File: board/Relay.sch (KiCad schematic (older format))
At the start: 9 parts, among them K1 JS1-12V-F, K2 JS1-12V-F, K3 JS1-12V-F, K4 JS1-12V-F, U4 ULN2003A

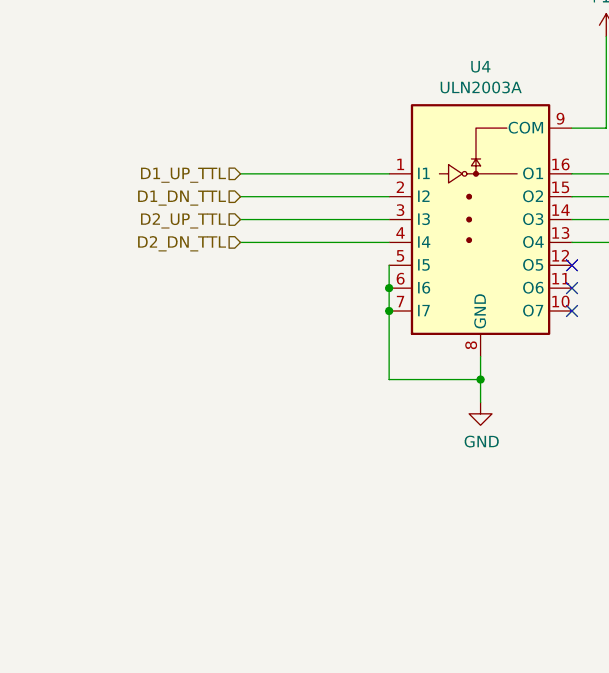
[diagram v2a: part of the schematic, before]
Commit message: Add relay status LEDs
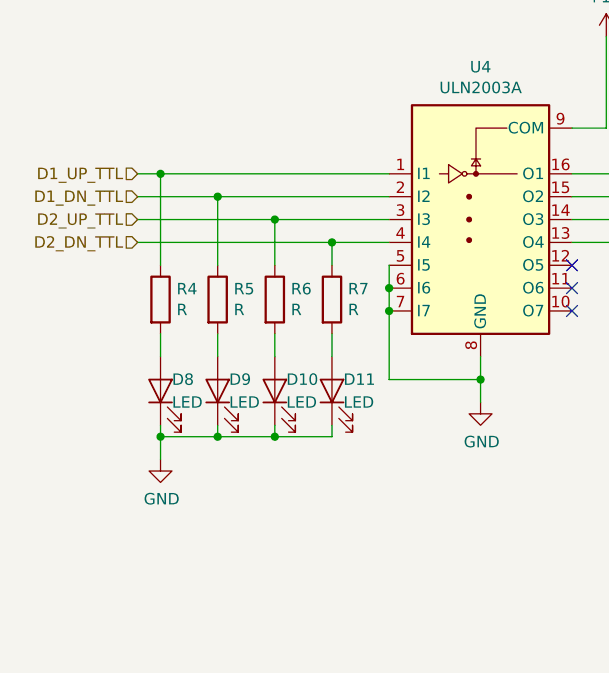
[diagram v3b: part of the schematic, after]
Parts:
- added D10, D11, D8, D9: LED, LEDs:LED_D3.0mm, symbol Device:LED
- added R4, R5, R6, R7: R, Resistors_THT:R_Axial_DIN0207_L6.3mm_D2.5mm_P10.16mm_Horizontal, symbol Device:R
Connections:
- net D1_DN_TTL: now also R5.1
- net D1_UP_TTL: now also R4.1
- net D2_DN_TTL: now also R7.1
- net D2_UP_TTL: now also R6.1
- net GND: now also D10.1 (K), D11.1 (K), D8.1 (K), D9.1 (K)
- new net: D11.2 (A), R7.2
- new net: D10.2 (A), R6.2
- new net: D9.2 (A), R5.2
- new net: D8.2 (A), R4.2
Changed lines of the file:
@@
 	1    0    0    -1
 $EndComp
-Text HLabel 1500 2500 0    50   Input ~ 0
+Text HLabel 1050 2500 0    50   Input ~ 0
 D1_UP_TTL
-Text HLabel 1500 2600 0    50   Input ~ 0
+Text HLabel 1050 2600 0    50   Input ~ 0
 D1_DN_TTL
-Text HLabel 1500 2700 0    50   Input ~ 0
+Text HLabel 1050 2700 0    50   Input ~ 0
 D2_UP_TTL
-Text HLabel 1500 2800 0    50   Input ~ 0
+Text HLabel 1050 2800 0    50   Input ~ 0
 D2_DN_TTL
-Wire Wire Line
-	1500 2500 2150 2500
-Wire Wire Line
-	1500 2600 2150 2600
-Wire Wire Line
-	1500 2700 2150 2700
-Wire Wire Line
-	1500 2800 2150 2800
 $Comp
 L power:GND #PWR0106
@@
 Wire Wire Line
 	7850 3300 7850 4300
+Wire Wire Line
+	1050 2500 1150 2500
+Wire Wire Line
+	1050 2600 1400 2600
+Wire Wire Line
+	1050 2700 1650 2700
+Wire Wire Line
+	1050 2800 1900 2800
+$Comp
+L Device:R R7
+U 1 1 5D6E4821
+P 1900 3050
+F 0 "R7" H 1970 3096 50  0000 L CNN
+F 1 "R" H 1970 3005 50  0000 L CNN
+F 2 "Resistors_THT:R_Axial_DIN0207_L6.3mm_D2.5mm_P10.16mm_Horizontal" V 1830 3050 50  0001 C CNN
+F 3 "~" H 1900 3050 50  0001 C CNN
+	1    1900 3050
+	1    0    0    -1
+$EndComp
+$Comp
+L Device:R R6
+U 1 1 5D6E54AB
+P 1650 3050
+F 0 "R6" H 1720 3096 50  0000 L CNN
+F 1 "R" H 1720 3005 50  0000 L CNN
+F 2 "Resistors_THT:R_Axial_DIN0207_L6.3mm_D2.5mm_P10.16mm_Horizontal" V 1580 3050 50  0001 C CNN
+F 3 "~" H 1650 3050 50  0001 C CNN
+	1    1650 3050
+	1    0    0    -1
+$EndComp
+$Comp
+L Device:R R5
+U 1 1 5D6E6CF6
+P 1400 3050
+F 0 "R5" H 1470 3096 50  0000 L CNN
+F 1 "R" H 1470 3005 50  0000 L CNN
+F 2 "Resistors_THT:R_Axial_DIN0207_L6.3mm_D2.5mm_P10.16mm_Horizontal" V 1330 3050 50  0001 C CNN
+F 3 "~" H 1400 3050 50  0001 C CNN
+	1    1400 3050
+	1    0    0    -1
+$EndComp
+$Comp
+L Device:R R4
+U 1 1 5D6E8437
+P 1150 3050
+F 0 "R4" H 1220 3096 50  0000 L CNN
+F 1 "R" H 1220 3005 50  0000 L CNN
+F 2 "Resistors_THT:R_Axial_DIN0207_L6.3mm_D2.5mm_P10.16mm_Horizontal" V 1080 3050 50  0001 C CNN
+F 3 "~" H 1150 3050 50  0001 C CNN
+	1    1150 3050
+	1    0    0    -1
+$EndComp
+$Comp
+L Device:LED D8
+U 1 1 5D6E9A8E
+P 1150 3450
+F 0 "D8" V 1200 3400 50  0000 R CNN
+F 1 "LED" V 1100 3400 50  0000 R CNN
+F 2 "LEDs:LED_D3.0mm" H 1150 3450 50  0001 C CNN
+F 3 "~" H 1150 3450 50  0001 C CNN
+	1    1150 3450
+	0    -1   -1   0
+$EndComp
+$Comp
+L Device:LED D9
+U 1 1 5D6EA810
+P 1400 3450
+F 0 "D9" V 1450 3400 50  0000 R CNN
+F 1 "LED" V 1350 3400 50  0000 R CNN
+F 2 "LEDs:LED_D3.0mm" H 1400 3450 50  0001 C CNN
+F 3 "~" H 1400 3450 50  0001 C CNN
+	1    1400 3450
+	0    -1   -1   0
+$EndComp
+$Comp
+L Device:LED D10
+U 1 1 5D6EC3F0
+P 1650 3450
+F 0 "D10" V 1700 3400 50  0000 R CNN
+F 1 "LED" V 1600 3400 50  0000 R CNN
+F 2 "LEDs:LED_D3.0mm" H 1650 3450 50  0001 C CNN
+F 3 "~" H 1650 3450 50  0001 C CNN
+	1    1650 3450
+	0    -1   -1   0
+$EndComp
+$Comp
+L Device:LED D11
+U 1 1 5D6EE0A2
+P 1900 3450
+F 0 "D11" V 1950 3400 50  0000 R CNN
+F 1 "LED" V 1850 3400 50  0000 R CNN
+F 2 "LEDs:LED_D3.0mm" H 1900 3450 50  0001 C CNN
+F 3 "~" H 1900 3450 50  0001 C CNN
+	1    1900 3450
+	0    -1   -1   0
+$EndComp
+Wire Wire Line
+	1150 2500 1150 2900
+Connection ~ 1150 2500
+Wire Wire Line
+	1150 2500 2150 2500
+Wire Wire Line
+	1400 2600 1400 2900
+Connection ~ 1400 2600
+Wire Wire Line
+	1400 2600 2150 2600
+Wire Wire Line
+	1650 2700 1650 2900
+Connection ~ 1650 2700
+Wire Wire Line
+	1650 2700 2150 2700
+Wire Wire Line
+	1900 2800 1900 2900
+Connection ~ 1900 2800
+Wire Wire Line
+	1900 2800 2150 2800
+Wire Wire Line
+	1150 3200 1150 3300
+Wire Wire Line
+	1400 3200 1400 3300
+Wire Wire Line
+	1650 3200 1650 3300
+Wire Wire Line
+	1900 3200 1900 3300
+$Comp
+L power:GND #PWR0110
+U 1 1 5D700BE5
+P 1150 3750
+F 0 "#PWR0110" H 1150 3500 50  0001 C CNN
+F 1 "GND" H 1155 3577 50  0000 C CNN
+F 2 "" H 1150 3750 50  0001 C CNN
+F 3 "" H 1150 3750 50  0001 C CNN
+	1    1150 3750
+	1    0    0    -1
+$EndComp
+Wire Wire Line
+	1150 3600 1150 3650
+Wire Wire Line
+	1400 3600 1400 3650
+Wire Wire Line
+	1400 3650 1150 3650
+Connection ~ 1150 3650
+Wire Wire Line
+	1150 3650 1150 3750
+Wire Wire Line
+	1650 3600 1650 3650
+Wire Wire Line
+	1650 3650 1400 3650
+Connection ~ 1400 3650
+Wire Wire Line
+	1900 3600 1900 3650
+Wire Wire Line
+	1900 3650 1650 3650
+Connection ~ 1650 3650
 $EndSCHEMATC

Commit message: Add nominal LED R values; ground plane tweaks; first board spin
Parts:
- R4, R5, R6, R7: value R -> 150R
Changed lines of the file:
@@
 P 1900 3050
 F 0 "R7" H 1970 3096 50  0000 L CNN
-F 1 "R" H 1970 3005 50  0000 L CNN
+F 1 "150R" V 1900 2950 50  0000 L CNN
 F 2 "Resistors_THT:R_Axial_DIN0207_L6.3mm_D2.5mm_P10.16mm_Horizontal" V 1830 3050 50  0001 C CNN
 F 3 "~" H 1900 3050 50  0001 C CNN
@@
 P 1650 3050
 F 0 "R6" H 1720 3096 50  0000 L CNN
-F 1 "R" H 1720 3005 50  0000 L CNN
+F 1 "150R" V 1650 2950 50  0000 L CNN
 F 2 "Resistors_THT:R_Axial_DIN0207_L6.3mm_D2.5mm_P10.16mm_Horizontal" V 1580 3050 50  0001 C CNN
 F 3 "~" H 1650 3050 50  0001 C CNN
@@
 P 1400 3050
 F 0 "R5" H 1470 3096 50  0000 L CNN
-F 1 "R" H 1470 3005 50  0000 L CNN
+F 1 "150R" V 1400 2950 50  0000 L CNN
 F 2 "Resistors_THT:R_Axial_DIN0207_L6.3mm_D2.5mm_P10.16mm_Horizontal" V 1330 3050 50  0001 C CNN
 F 3 "~" H 1400 3050 50  0001 C CNN
@@
 P 1150 3050
 F 0 "R4" H 1220 3096 50  0000 L CNN
-F 1 "R" H 1220 3005 50  0000 L CNN
+F 1 "150R" V 1150 2950 50  0000 L CNN
 F 2 "Resistors_THT:R_Axial_DIN0207_L6.3mm_D2.5mm_P10.16mm_Horizontal" V 1080 3050 50  0001 C CNN
 F 3 "~" H 1150 3050 50  0001 C CNN

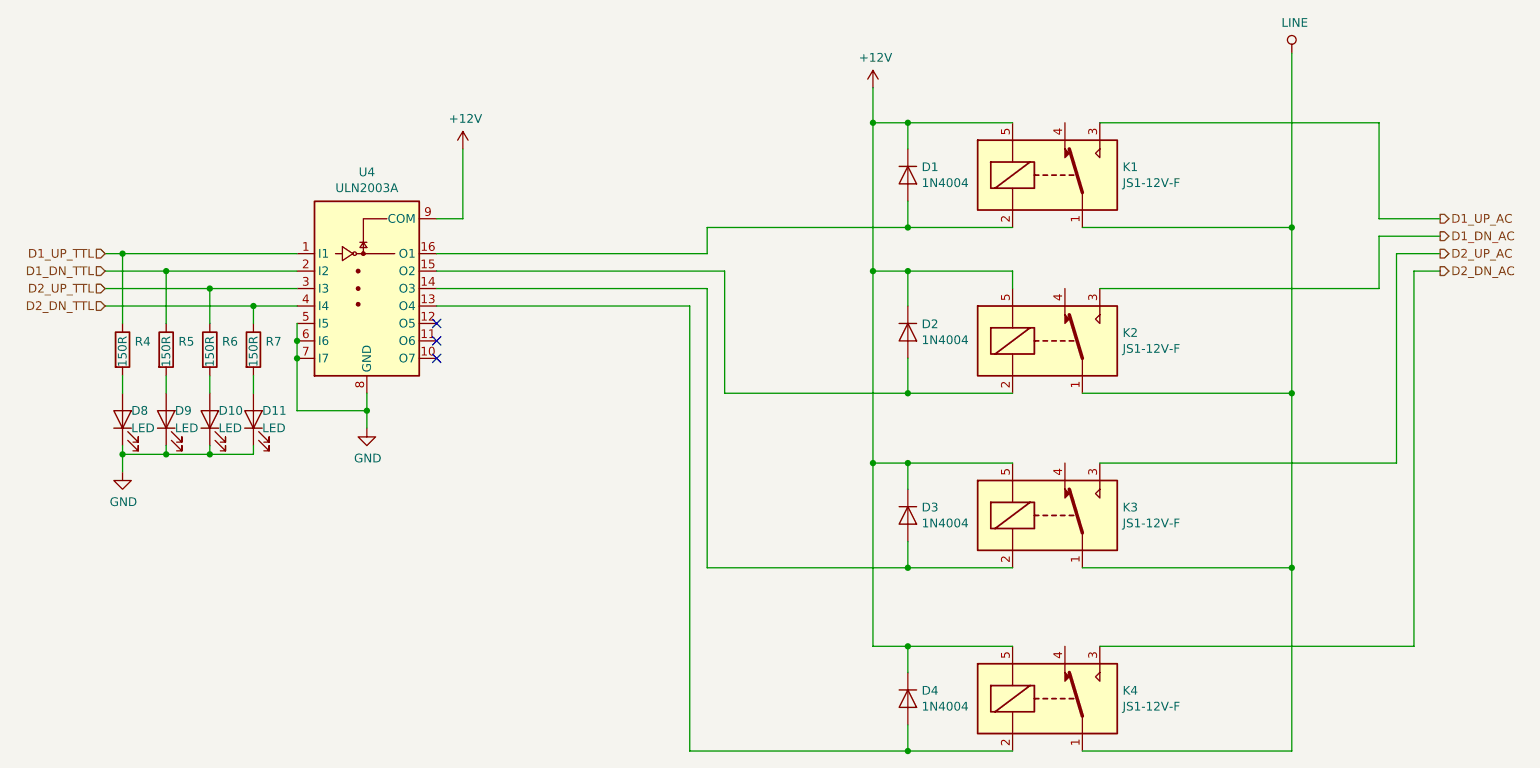
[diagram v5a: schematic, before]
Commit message: Minor layout tweaks, component updates
* Add an MCU driven status LED
* Update LED current limit resistor values
* Minor trace tweaks for clearance
* Based on empirical measurements of rev 0.1 board, adjust the location of the
  board mounting holes.
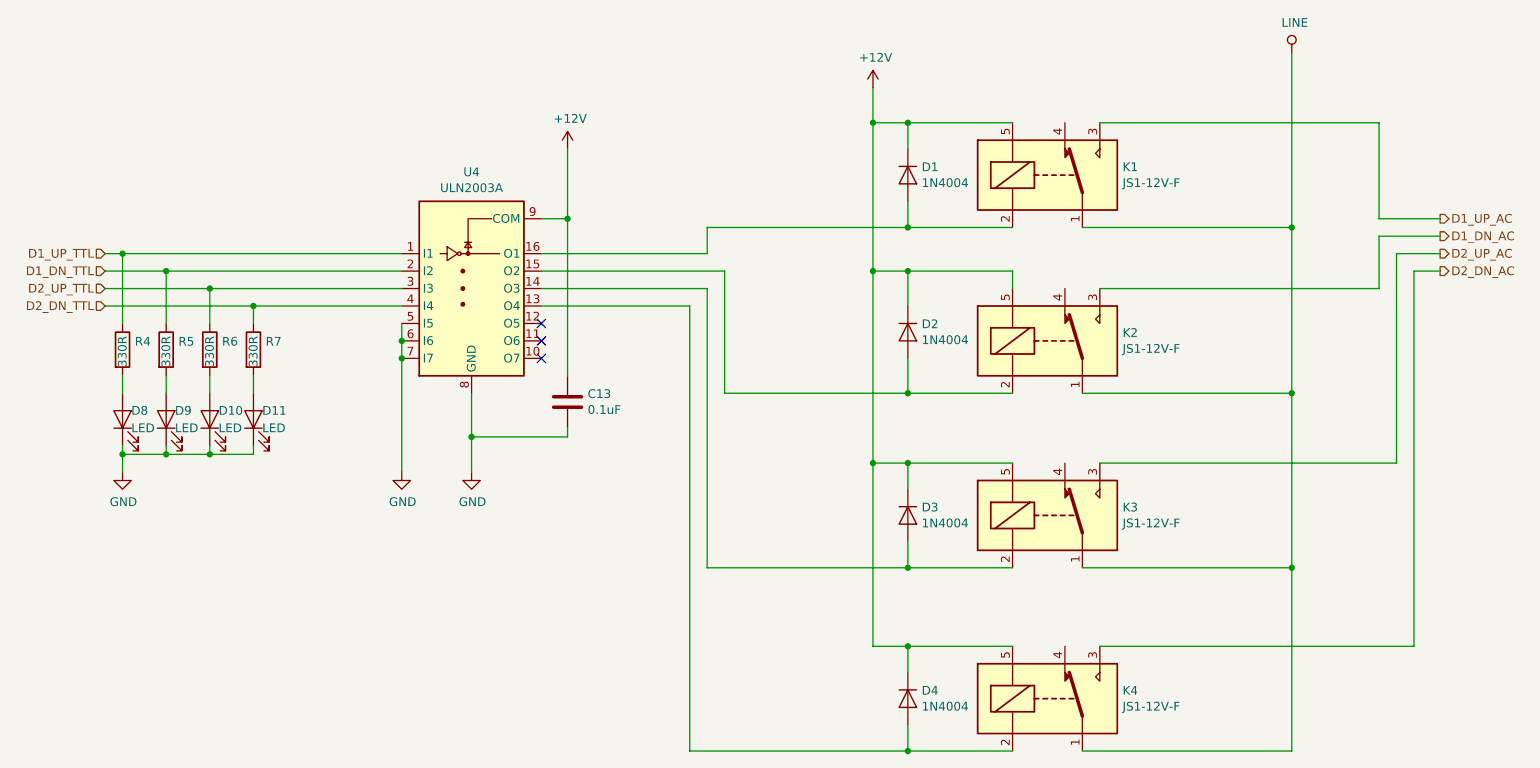
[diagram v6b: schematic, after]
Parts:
- added C13: 0.1uF, Capacitors_THT:C_Disc_D5.0mm_W2.5mm_P2.50mm, symbol Device:C
- R4, R5, R6, R7: value 150R -> 330R
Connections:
- net +12V: now also C13.1
- net GND: now also C13.2
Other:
- moved on the sheet: U4
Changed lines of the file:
@@
 L Transistor_Array:ULN2003A U4
 U 1 1 5D6FD156
-P 2550 2700
-F 0 "U4" H 2550 3367 50  0000 C CNN
-F 1 "ULN2003A" H 2550 3276 50  0000 C CNN
-F 2 "Housings_DIP:DIP-16_W7.62mm_LongPads" H 2600 2150 50  0001 L CNN
-F 3 "http://www.ti.com/lit/ds/symlink/uln2003a.pdf" H 2650 2500 50  0001 C CNN
-	1    2550 2700
+P 3150 2700
+F 0 "U4" H 3150 3367 50  0000 C CNN
+F 1 "ULN2003A" H 3150 3276 50  0000 C CNN
+F 2 "Housings_DIP:DIP-16_W7.62mm_LongPads" H 3200 2150 50  0001 L CNN
+F 3 "http://www.ti.com/lit/ds/symlink/uln2003a.pdf" H 3250 2500 50  0001 C CNN
+	1    3150 2700
 	1    0    0    -1
 $EndComp
@@
 L power:GND #PWR0106
 U 1 1 5D7017FB
-P 2550 3500
-F 0 "#PWR0106" H 2550 3250 50  0001 C CNN
-F 1 "GND" H 2555 3327 50  0000 C CNN
-F 2 "" H 2550 3500 50  0001 C CNN
-F 3 "" H 2550 3500 50  0001 C CNN
-	1    2550 3500
-	1    0    0    -1
-$EndComp
-Wire Wire Line
-	2550 3300 2550 3400
+P 3150 3750
+F 0 "#PWR0106" H 3150 3500 50  0001 C CNN
+F 1 "GND" H 3155 3577 50  0000 C CNN
+F 2 "" H 3150 3750 50  0001 C CNN
+F 3 "" H 3150 3750 50  0001 C CNN
+	1    3150 3750
+	1    0    0    -1
+$EndComp
 $Comp
 L power:+12V #PWR0107
 U 1 1 5D701C71
-P 3100 1900
-F 0 "#PWR0107" H 3100 1750 50  0001 C CNN
-F 1 "+12V" H 3115 2073 50  0000 C CNN
-F 2 "" H 3100 1900 50  0001 C CNN
-F 3 "" H 3100 1900 50  0001 C CNN
-	1    3100 1900
-	1    0    0    -1
-$EndComp
-Wire Wire Line
-	2950 2300 3100 2300
-Wire Wire Line
-	3100 2300 3100 1900
-Wire Wire Line
-	2150 2900 2150 3000
-Wire Wire Line
-	2150 3000 2150 3100
-Connection ~ 2150 3000
-Wire Wire Line
-	2150 3100 2150 3400
-Wire Wire Line
-	2150 3400 2550 3400
-Connection ~ 2150 3100
-Connection ~ 2550 3400
-Wire Wire Line
-	2550 3400 2550 3500
-NoConn ~ 2950 2900
-NoConn ~ 2950 3000
-NoConn ~ 2950 3100
+P 3700 1900
+F 0 "#PWR0107" H 3700 1750 50  0001 C CNN
+F 1 "+12V" H 3715 2073 50  0000 C CNN
+F 2 "" H 3700 1900 50  0001 C CNN
+F 3 "" H 3700 1900 50  0001 C CNN
+	1    3700 1900
+	1    0    0    -1
+$EndComp
+Wire Wire Line
+	3550 2300 3700 2300
+Wire Wire Line
+	3700 2300 3700 1900
+Wire Wire Line
+	2750 2900 2750 3000
+Wire Wire Line
+	2750 3000 2750 3100
+Connection ~ 2750 3000
+NoConn ~ 3550 2900
+NoConn ~ 3550 3000
+NoConn ~ 3550 3100
 Text HLabel 8700 2300 2    50   Output ~ 0
 D1_UP_AC
@@
 	6250 2350 5650 2350
 Wire Wire Line
-	2950 2500 4500 2500
-Wire Wire Line
 	6250 2600 6250 2700
-Wire Wire Line
-	2950 2700 4500 2700
-Wire Wire Line
-	2950 2800 4400 2800
 $Comp
 L Diode:1N4004 D1
@@
 Wire Wire Line
 	4600 3300 4600 2600
-Wire Wire Line
-	4600 2600 2950 2600
 Connection ~ 5650 3300
 $Comp
@@
 P 1900 3050
 F 0 "R7" H 1970 3096 50  0000 L CNN
-F 1 "150R" V 1900 2950 50  0000 L CNN
+F 1 "330R" V 1900 2950 50  0000 L CNN
 F 2 "Resistors_THT:R_Axial_DIN0207_L6.3mm_D2.5mm_P10.16mm_Horizontal" V 1830 3050 50  0001 C CNN
 F 3 "~" H 1900 3050 50  0001 C CNN
@@
 P 1650 3050
 F 0 "R6" H 1720 3096 50  0000 L CNN
-F 1 "150R" V 1650 2950 50  0000 L CNN
+F 1 "330R" V 1650 2950 50  0000 L CNN
 F 2 "Resistors_THT:R_Axial_DIN0207_L6.3mm_D2.5mm_P10.16mm_Horizontal" V 1580 3050 50  0001 C CNN
 F 3 "~" H 1650 3050 50  0001 C CNN
@@
 P 1400 3050
 F 0 "R5" H 1470 3096 50  0000 L CNN
-F 1 "150R" V 1400 2950 50  0000 L CNN
+F 1 "330R" V 1400 2950 50  0000 L CNN
 F 2 "Resistors_THT:R_Axial_DIN0207_L6.3mm_D2.5mm_P10.16mm_Horizontal" V 1330 3050 50  0001 C CNN
 F 3 "~" H 1400 3050 50  0001 C CNN
 	1    1400 3050
-	1    0    0    -1
-$EndComp
-$Comp
-L Device:R R4
-U 1 1 5D6E8437
-P 1150 3050
-F 0 "R4" H 1220 3096 50  0000 L CNN
-F 1 "150R" V 1150 2950 50  0000 L CNN
-F 2 "Resistors_THT:R_Axial_DIN0207_L6.3mm_D2.5mm_P10.16mm_Horizontal" V 1080 3050 50  0001 C CNN
-F 3 "~" H 1150 3050 50  0001 C CNN
-	1    1150 3050
 	1    0    0    -1
 $EndComp
@@
 Wire Wire Line
 	1150 2500 1150 2900
-Connection ~ 1150 2500
-Wire Wire Line
-	1150 2500 2150 2500
 Wire Wire Line
 	1400 2600 1400 2900
-Connection ~ 1400 2600
-Wire Wire Line
-	1400 2600 2150 2600
 Wire Wire Line
 	1650 2700 1650 2900
-Connection ~ 1650 2700
-Wire Wire Line
-	1650 2700 2150 2700
 Wire Wire Line
 	1900 2800 1900 2900
-Connection ~ 1900 2800
-Wire Wire Line
-	1900 2800 2150 2800
 Wire Wire Line
 	1150 3200 1150 3300
@@
 	1900 3650 1650 3650
 Connection ~ 1650 3650
+$Comp
+L Device:R R4
+U 1 1 5D6E8437
+P 1150 3050
+F 0 "R4" H 1220 3096 50  0000 L CNN
+F 1 "330R" V 1150 2950 50  0000 L CNN
+F 2 "Resistors_THT:R_Axial_DIN0207_L6.3mm_D2.5mm_P10.16mm_Horizontal" V 1080 3050 50  0001 C CNN
+F 3 "~" H 1150 3050 50  0001 C CNN
+	1    1150 3050
+	1    0    0    -1
+$EndComp
+$Comp
+L power:GND #PWR0112
+U 1 1 5D758D65
+P 2750 3750
+F 0 "#PWR0112" H 2750 3500 50  0001 C CNN
+F 1 "GND" H 2755 3577 50  0000 C CNN
+F 2 "" H 2750 3750 50  0001 C CNN
+F 3 "" H 2750 3750 50  0001 C CNN
+	1    2750 3750
+	1    0    0    -1
+$EndComp
+Wire Wire Line
+	3150 3300 3150 3550
+Wire Wire Line
+	2750 3100 2750 3750
+Connection ~ 2750 3100
+Wire Wire Line
+	3550 2500 4500 2500
+Wire Wire Line
+	3550 2600 4600 2600
+Wire Wire Line
+	3550 2700 4500 2700
+Wire Wire Line
+	3550 2800 4400 2800
+Wire Wire Line
+	2750 2500 1150 2500
+Connection ~ 1150 2500
+Wire Wire Line
+	2750 2600 1400 2600
+Connection ~ 1400 2600
+Wire Wire Line
+	2750 2700 1650 2700
+Connection ~ 1650 2700
+Wire Wire Line
+	2750 2800 1900 2800
+Connection ~ 1900 2800
+$Comp
+L Device:C C13
+U 1 1 5D7871B3
+P 3700 3350
+F 0 "C13" H 3815 3396 50  0000 L CNN
+F 1 "0.1uF" H 3815 3305 50  0000 L CNN
+F 2 "Capacitors_THT:C_Disc_D5.0mm_W2.5mm_P2.50mm" H 3738 3200 50  0001 C CNN
+F 3 "~" H 3700 3350 50  0001 C CNN
+	1    3700 3350
+	1    0    0    -1
+$EndComp
+Wire Wire Line
+	3700 2300 3700 3200
+Connection ~ 3700 2300
+Wire Wire Line
+	3700 3500 3700 3550
+Wire Wire Line
+	3700 3550 3150 3550
+Connection ~ 3150 3550
+Wire Wire Line
+	3150 3550 3150 3750
 $EndSCHEMATC

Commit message: Split the 5v and 12v ground paths
* To control the return path for (noisy) relay current, split the grounds for
  the 12v and 5v sections.
* The grounds are joined by bridges (solder pads) placed adjacent to the 5v
  regulator, on both layers.
* The gound plane is split in two; conveniently the 12v vs 5v components were
  already well placed to make this straightforward.
* 12v power LED uses the 5v ground to simplify routing.
* Add dummy power flags for ERC
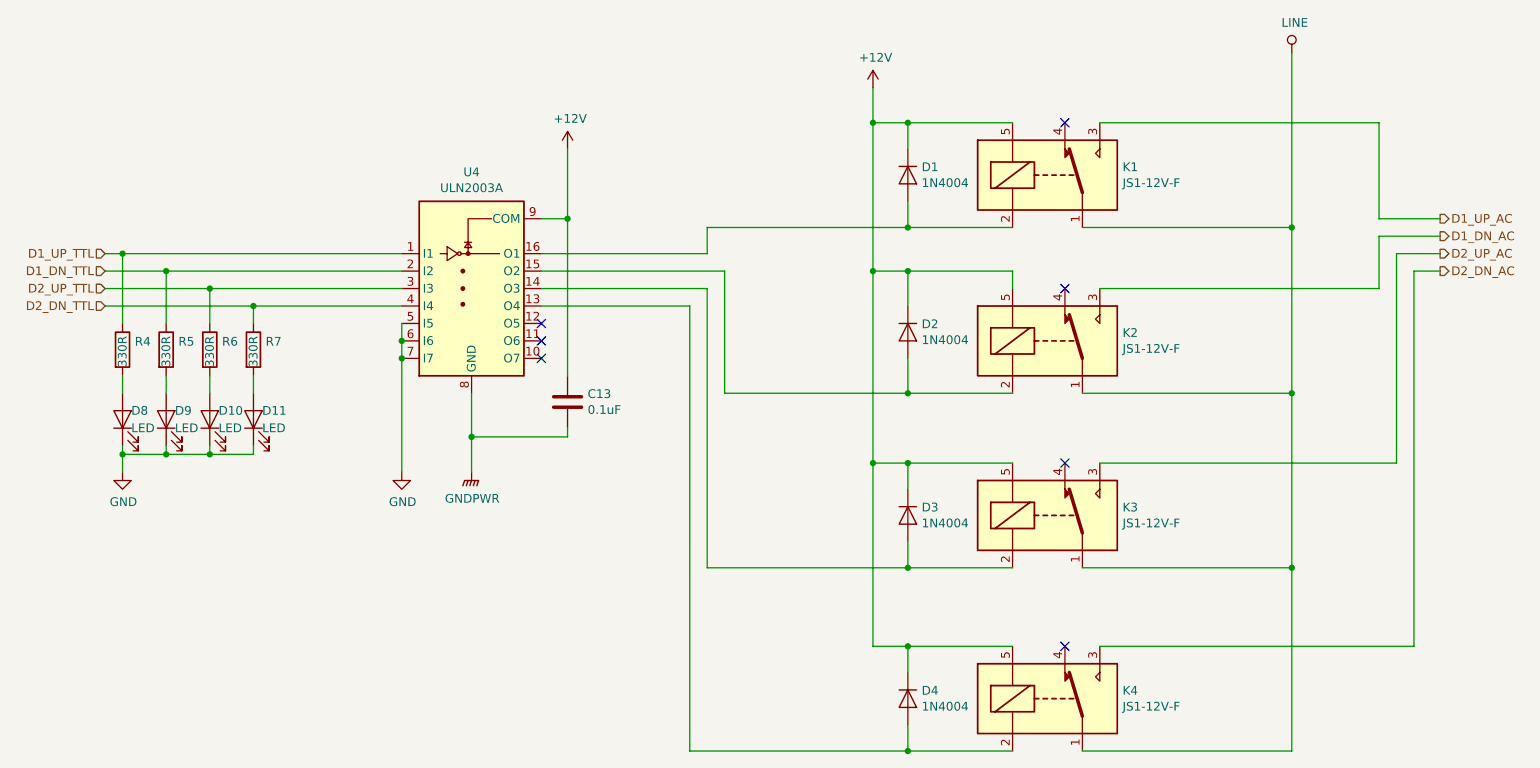
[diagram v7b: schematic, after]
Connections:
- net GND: no longer C13.2, U4.8 (GND)
- new net GNDPWR: C13.2, U4.8 (GND)
- no-connect marks 3 -> 7
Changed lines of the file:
@@
 Sheet 3 4
 Title "Projector Screen Controller"
-Date "2019-09-02"
+Date "2019-09-07"
 Rev "0.2"
 Comp "Flirble Open Source"
@@
 Text HLabel 1050 2800 0    50   Input ~ 0
 D2_DN_TTL
-$Comp
-L power:GND #PWR0106
-U 1 1 5D7017FB
-P 3150 3750
-F 0 "#PWR0106" H 3150 3500 50  0001 C CNN
-F 1 "GND" H 3155 3577 50  0000 C CNN
-F 2 "" H 3150 3750 50  0001 C CNN
-F 3 "" H 3150 3750 50  0001 C CNN
-	1    3150 3750
-	1    0    0    -1
-$EndComp
 $Comp
 L power:+12V #PWR0107
@@
 Wire Wire Line
 	3150 3550 3150 3750
+$Comp
+L power:GNDPWR #PWR012
+U 1 1 5D7B0E70
+P 3150 3750
+F 0 "#PWR012" H 3150 3550 50  0001 C CNN
+F 1 "GNDPWR" H 3154 3596 50  0000 C CNN
+F 2 "" H 3150 3700 50  0001 C CNN
+F 3 "" H 3150 3700 50  0001 C CNN
+	1    3150 3750
+	1    0    0    -1
+$EndComp
+NoConn ~ 6550 1750
+NoConn ~ 6550 2700
+NoConn ~ 6550 3700
+NoConn ~ 6550 4750
 $EndSCHEMATC
